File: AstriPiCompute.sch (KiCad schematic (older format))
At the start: 36 parts, among them J01_OUT1 12V, J02_OUT1 12V, J03_OUT1 12V, Q1 TIP3055, Q2 TIP122, Q3 TIP122, U1 IRF7313, U2 MP1584EN-LF-Z

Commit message: Major PCB changes. Termal releaf areas added
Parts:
- removed D1: BAS116T, BAS116T:SOT416, symbol BAS116T:BAS116T
- added D1: 1N4001, Diode_SMD:D_0805_2012Metric_Pad1.15x1.40mm_HandSolder, symbol Diode:1N4001
- added TP_5V1, TP_GND1: TestPoint_Flag, TestPoint:TestPoint_Pad_1.0x1.0mm, symbol Connector:TestPoint_Flag
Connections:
- wire segments 98 -> 101
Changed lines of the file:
@@
 Text Label 1700 4150 0    50   ~ 0
 IN_GND
-$Comp
-L BAS116T:BAS116T D1
-U 1 1 5D597852
-P 3700 2800
-F 0 "D1" V 3746 2720 50  0000 R CNN
-F 1 "BAS116T" V 3655 2720 50  0000 R CNN
-F 2 "BAS116T:SOT416" H 3700 2800 50  0001 L BNN
-F 3 "BAS116" H 3700 2800 50  0001 L BNN
-F 4 "Unavailable" H 3700 2800 50  0001 L BNN "Campo4"
-F 5 "SOT-23 Infineon" H 3700 2800 50  0001 L BNN "Campo5"
-F 6 "Diode 85V 250mA Low Leakage SOT23" H 3700 2800 50  0001 L BNN "Campo6"
-F 7 "Infineon" H 3700 2800 50  0001 L BNN "Campo7"
-F 8 "None" H 3700 2800 50  0001 L BNN "Campo8"
-	1    3700 2800
-	0    -1   -1   0
-$EndComp
 Wire Wire Line
 	3700 3150 3700 2900
-Wire Wire Line
-	3700 2700 3700 2400
 Wire Wire Line
 	3700 2400 3200 2400
@@
 L power:GND #PWR09
 U 1 1 5D759508
-P 10100 3550
-F 0 "#PWR09" H 10100 3300 50  0001 C CNN
-F 1 "GND" H 10105 3377 50  0000 C CNN
-F 2 "" H 10100 3550 50  0001 C CNN
-F 3 "" H 10100 3550 50  0001 C CNN
-	1    10100 3550
+P 10100 3750
+F 0 "#PWR09" H 10100 3500 50  0001 C CNN
+F 1 "GND" H 10105 3577 50  0000 C CNN
+F 2 "" H 10100 3750 50  0001 C CNN
+F 3 "" H 10100 3750 50  0001 C CNN
+	1    10100 3750
 	1    0    0    -1
 $EndComp
@@
 Wire Wire Line
 	2650 2400 2600 2400
+$Comp
+L Diode:1N4001 D1
+U 1 1 5E32FC19
+P 3700 2750
+F 0 "D1" V 3654 2829 50  0000 L CNN
+F 1 "1N4001" V 3745 2829 50  0000 L CNN
+F 2 "Diode_SMD:D_0805_2012Metric_Pad1.15x1.40mm_HandSolder" H 3700 2575 50  0001 C CNN
+F 3 "http://www.vishay.com/docs/88503/1n4001.pdf" H 3700 2750 50  0001 C CNN
+	1    3700 2750
+	0    1    1    0
+$EndComp
+Wire Wire Line
+	3700 2700 3700 2600
+Wire Wire Line
+	3700 2400 3700 2600
+Connection ~ 3700 2600
+$Comp
+L Connector:TestPoint_Flag TP_5V1
+U 1 1 5E35CCBD
+P 10100 3150
+F 0 "TP_5V1" H 10360 3244 50  0000 L CNN
+F 1 "TestPoint_Flag" H 10360 3153 50  0000 L CNN
+F 2 "TestPoint:TestPoint_Pad_1.0x1.0mm" H 10300 3150 50  0001 C CNN
+F 3 "~" H 10300 3150 50  0001 C CNN
+	1    10100 3150
+	1    0    0    -1
+$EndComp
+Connection ~ 10100 3150
+Wire Wire Line
+	10100 3550 10100 3700
+$Comp
+L Connector:TestPoint_Flag TP_GND1
+U 1 1 5E36BED7
+P 10100 3700
+F 0 "TP_GND1" H 10360 3794 50  0000 L CNN
+F 1 "TestPoint_Flag" H 10360 3703 50  0000 L CNN
+F 2 "TestPoint:TestPoint_Pad_1.0x1.0mm" H 10300 3700 50  0001 C CNN
+F 3 "~" H 10300 3700 50  0001 C CNN
+	1    10100 3700
+	1    0    0    -1
+$EndComp
+Connection ~ 10100 3700
+Wire Wire Line
+	10100 3700 10100 3750
 $EndSCHEMATC

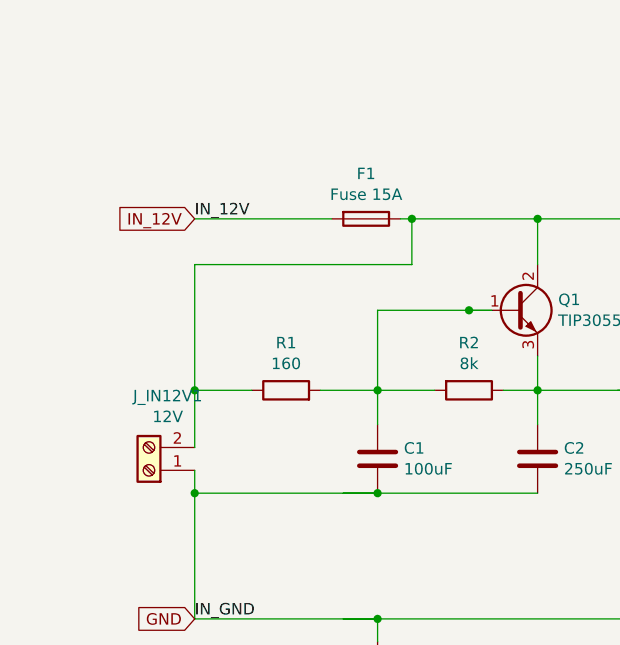
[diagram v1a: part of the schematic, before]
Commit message: Reworked 12V connectors  for 5mm size
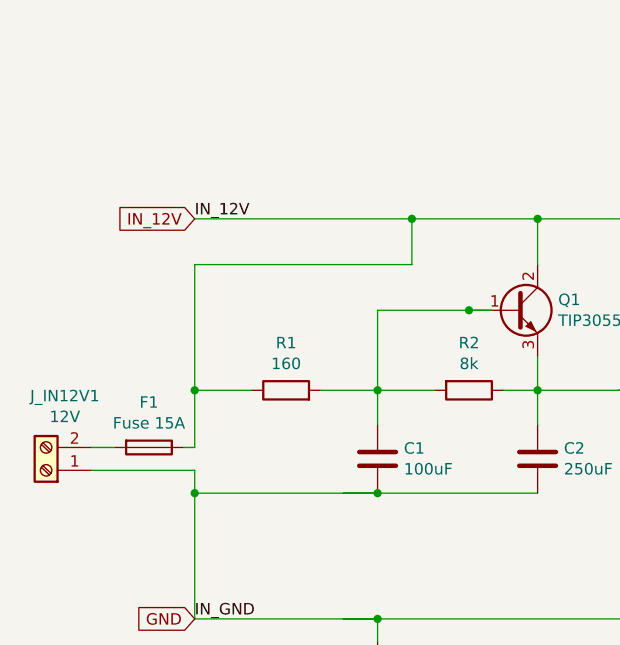
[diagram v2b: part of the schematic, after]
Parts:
- J01_OUT1, J02_OUT1, J03_OUT1, J_IN12V1: footprint Connector_Wire:SolderWirePad_1x02_P3.81mm_Drill0.8mm -> Connector_Wire:SolderWirePad_1x02_P5.08mm_Drill1.5mm
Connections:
- wire segments 101 -> 103
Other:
- moved on the sheet: F1, J_IN12V1
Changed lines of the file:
@@
 L Connector:Screw_Terminal_01x02 J_IN12V1
 U 1 1 5D594266
-P 1500 3500
-F 0 "J_IN12V1" H 1418 3175 50  0000 C CNN
-F 1 "12V" H 1418 3266 50  0000 C CNN
-F 2 "Connector_Wire:SolderWirePad_1x02_P3.81mm_Drill0.8mm" H 1500 3500 50  0001 C CNN
-F 3 "~" H 1500 3500 50  0001 C CNN
-	1    1500 3500
+P 1050 3500
+F 0 "J_IN12V1" H 968 3175 50  0000 C CNN
+F 1 "12V" H 968 3266 50  0000 C CNN
+F 2 "Connector_Wire:SolderWirePad_1x02_P5.08mm_Drill1.5mm" H 1050 3500 50  0001 C CNN
+F 3 "~" H 1050 3500 50  0001 C CNN
+	1    1050 3500
 	-1   0    0    1
 $EndComp
@@
 L Device:Fuse F1
 U 1 1 5D59995C
-P 2450 2400
-F 0 "F1" V 2253 2400 50  0000 C CNN
-F 1 "Fuse 15A" V 2344 2400 50  0000 C CNN
-F 2 "Fuse:Fuse_1206_3216Metric_Pad1.42x1.75mm_HandSolder" V 2380 2400 50  0001 C CNN
-F 3 "~" H 2450 2400 50  0001 C CNN
-	1    2450 2400
+P 1500 3400
+F 0 "F1" V 1303 3400 50  0000 C CNN
+F 1 "Fuse 15A" V 1394 3400 50  0000 C CNN
+F 2 "Fuse:Fuse_1206_3216Metric_Pad1.42x1.75mm_HandSolder" V 1430 3400 50  0001 C CNN
+F 3 "~" H 1500 3400 50  0001 C CNN
+	1    1500 3400
 	0    1    1    0
 $EndComp
-Wire Wire Line
-	2300 2400 1700 2400
 $Comp
 L Connector:Screw_Terminal_01x02 J01_OUT1
@@
 F 0 "J01_OUT1" H 3980 3792 50  0000 L CNN
 F 1 "12V" H 3980 3701 50  0000 L CNN
-F 2 "Connector_Wire:SolderWirePad_1x02_P3.81mm_Drill0.8mm" H 3900 3800 50  0001 C CNN
+F 2 "Connector_Wire:SolderWirePad_1x02_P5.08mm_Drill1.5mm" H 3900 3800 50  0001 C CNN
 F 3 "~" H 3900 3800 50  0001 C CNN
 	1    3900 3800
@@
 F 0 "J02_OUT1" H 4730 3792 50  0000 L CNN
 F 1 "12V" H 4730 3701 50  0000 L CNN
-F 2 "Connector_Wire:SolderWirePad_1x02_P3.81mm_Drill0.8mm" H 4650 3800 50  0001 C CNN
+F 2 "Connector_Wire:SolderWirePad_1x02_P5.08mm_Drill1.5mm" H 4650 3800 50  0001 C CNN
 F 3 "~" H 4650 3800 50  0001 C CNN
 	1    4650 3800
@@
 F 0 "J03_OUT1" H 5430 3792 50  0000 L CNN
 F 1 "12V" H 5430 3701 50  0000 L CNN
-F 2 "Connector_Wire:SolderWirePad_1x02_P3.81mm_Drill0.8mm" H 5350 3800 50  0001 C CNN
+F 2 "Connector_Wire:SolderWirePad_1x02_P5.08mm_Drill1.5mm" H 5350 3800 50  0001 C CNN
 F 3 "~" H 5350 3800 50  0001 C CNN
 	1    5350 3800
@@
 Connection ~ 1700 3150
 Connection ~ 2650 2400
-Wire Wire Line
-	2650 2400 2600 2400
 $Comp
 L Diode:1N4001 D1
@@
 Wire Wire Line
 	10100 3700 10100 3750
+Wire Wire Line
+	1700 2400 2650 2400
+Wire Wire Line
+	1700 3400 1650 3400
+Wire Wire Line
+	1250 3400 1350 3400
+Wire Wire Line
+	1700 3500 1250 3500
 $EndSCHEMATC
